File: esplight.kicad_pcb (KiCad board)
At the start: 2 copper layers, 14 parts, among them P1 CONN_01X03, P2 CONN_01X04, U1 AMS1117, U2 ESP-201

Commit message: got the board to a more or less finished state - gonna try variants now
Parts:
- removed USB1: BARREL_JACK, Connect:USB_Micro-B
- added P3: USB_B, Connect:USB_Micro-B, F.Cu at (27.9, 59.7)
- R1, R2, R3, R4: value 20kE -> 10kE
- SW1: renamed from BOOT; value DIPS_03 -> BOOT
- SW2: renamed from RESET; value SW_PUSH -> RESET
- moved U1 6.48 mm to (30.5, 50.8), turned to 180 degrees
- moved C2 2.54 mm to (34.3, 39.4)
- moved R3 2.50 mm to (25.4, 24.1)
- moved R2 1.78 mm to (25.4, 26.7)
- moved R1 1.63 mm to (25.4, 29.2)
- moved P2 1.48 mm to (41.9, 34.3)
- moved P1 1.30 mm to (41.9, 16.5)
- moved R4 1.27 mm to (25.4, 31.8)
- moved SW2 1.27 mm to (41.9, 43.2)
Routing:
- net GND: track 155.8 -> 137.4 mm
- net /3.3V: track 68.1 -> 55.1 mm
- net Net-(R1-Pad1): track 33.6 -> 40.2 mm
- net Net-(R3-Pad1): track 43.3 -> 48.3 mm
- net /+5V: track 53.0 -> 57.1 mm
- net Net-(P1-Pad1): track 18.0 -> 20.8 mm
- net Net-(P1-Pad2): track 16.1 -> 18.3 mm
- net Net-(R4-Pad1): track 14.3 -> 16.5 mm
- net Net-(R2-Pad1): track 44.5 -> 43.5 mm
- net Net-(P2-Pad2): track 5.18 -> 6.13 mm
- net (no net): track 0.00 -> 0.76 mm
- net Net-(P2-Pad3): track 7.72 -> 7.18 mm
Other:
- board outline added: 34.3 x 48.3 mm
- rule via_min_drill: 0.3 -> 0.35
- board text added: "GPIO 0"
- board text added: "GPIO 2"
- board text added: "GPIO15"
- board text added: "GPIO2 GPIO0 GPIO15 H L L Download H H L Boot Flash X X H Boot SD"
- board text added: "LED Control"
- board text added: "RESET"
- board text added: "Serial"

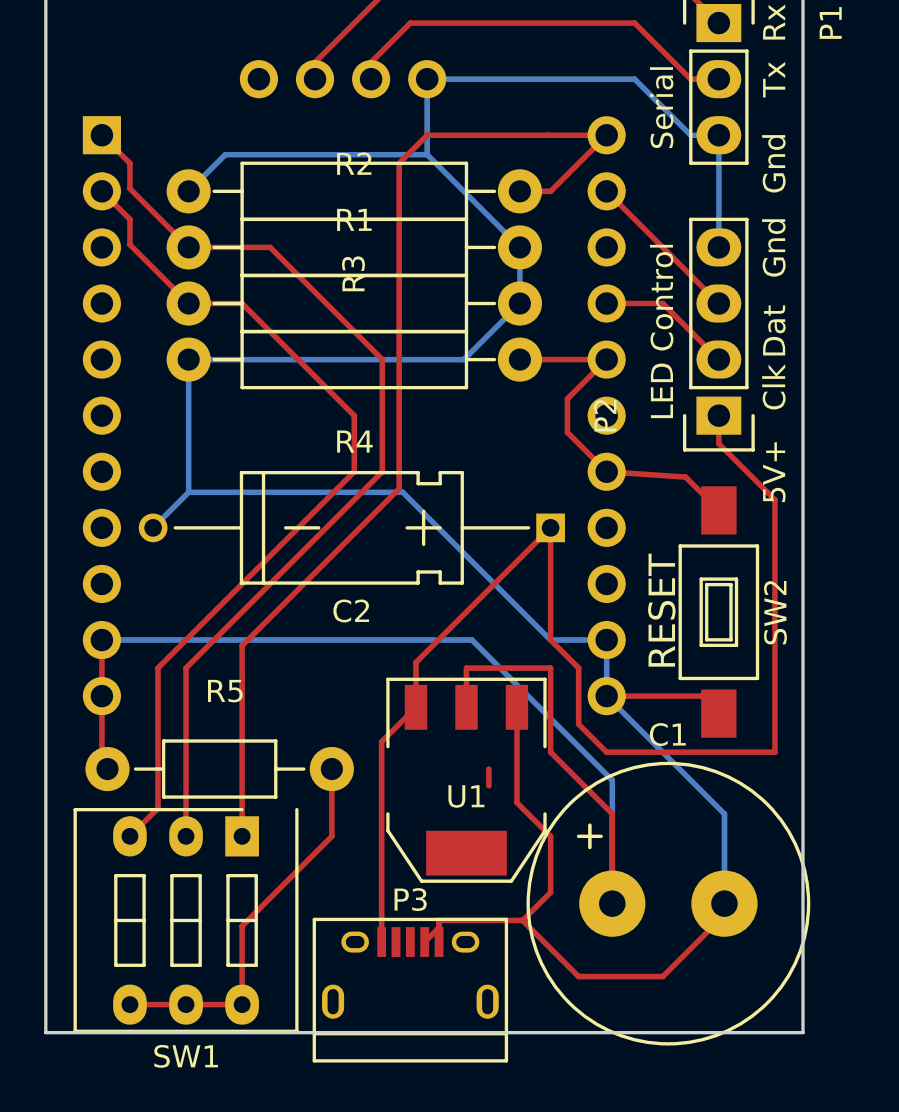
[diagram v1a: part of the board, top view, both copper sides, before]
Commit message: connecting chip_en pin, fixing some resistors
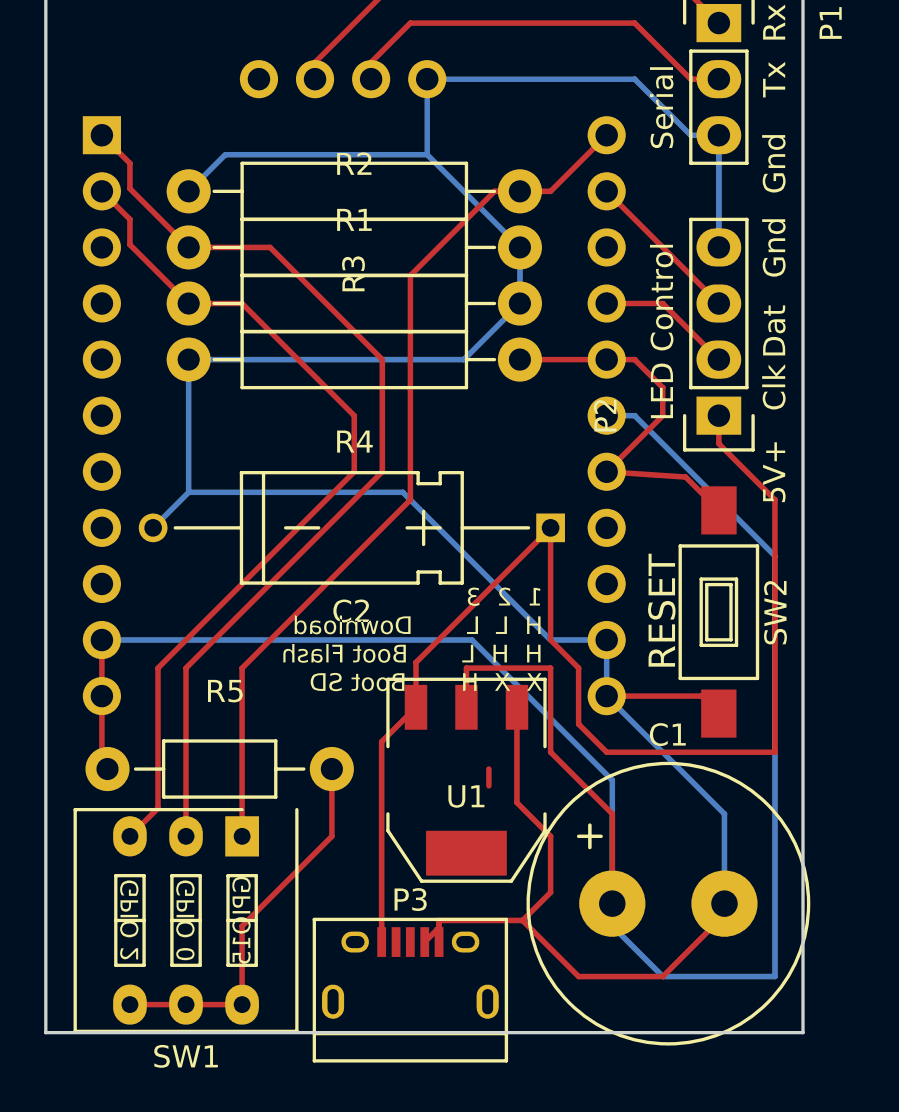
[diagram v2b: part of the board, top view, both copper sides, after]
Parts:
- R1, R2, R3, R4: value 10kE -> 1kE
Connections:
- U2 pad 17: /+3.3V -> /3.3V
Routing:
- net /3.3V: track 55.1 -> 93.7 mm
- net Net-(R3-Pad1): track 48.3 -> 40.1 mm
- net Net-(R4-Pad1): track 16.5 -> 17.9 mm
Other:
- board text added: "1 2 3 H L L Download H H L Boot Flash X X H Boot SD"
- board text removed: "GPIO2 GPIO0 GPIO15 H L L Download H H L Boot Flash X X H Boot SD"

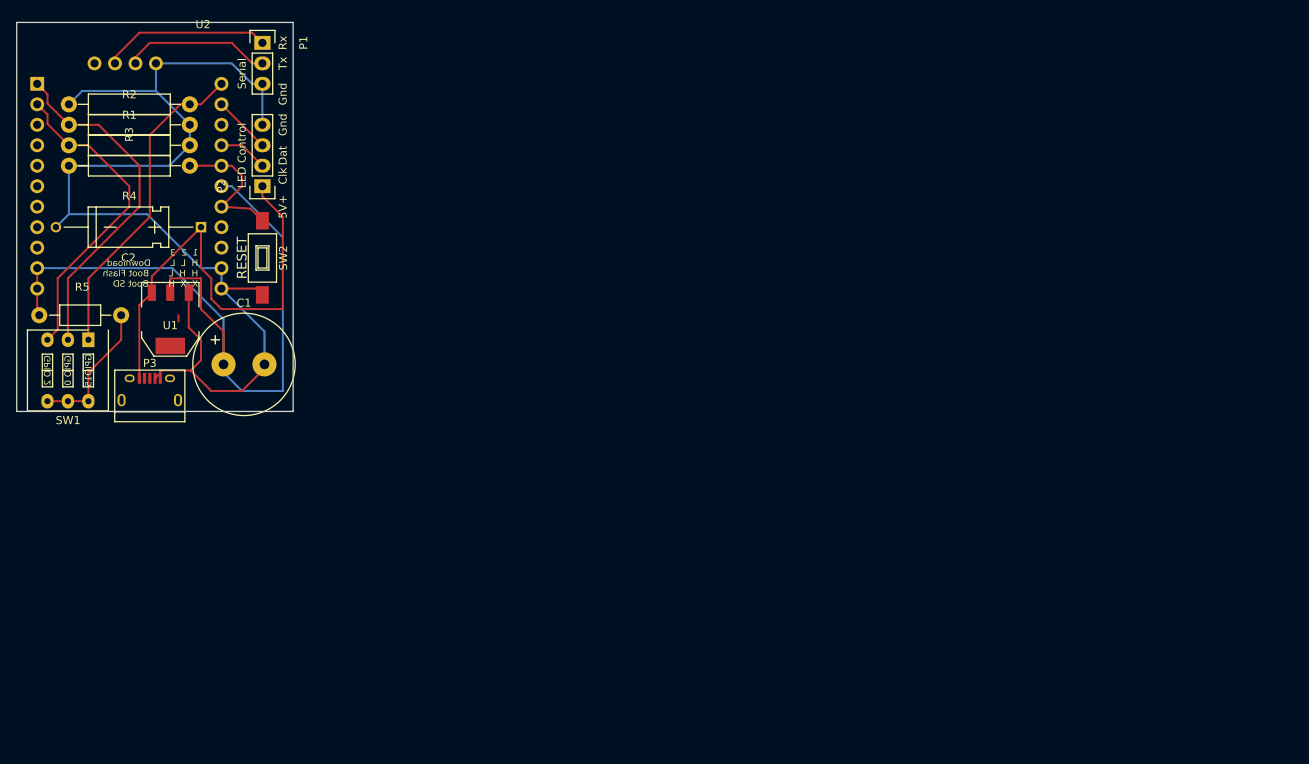
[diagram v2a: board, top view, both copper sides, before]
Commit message: Version 2 of the board - added USB/TTL and more SMT
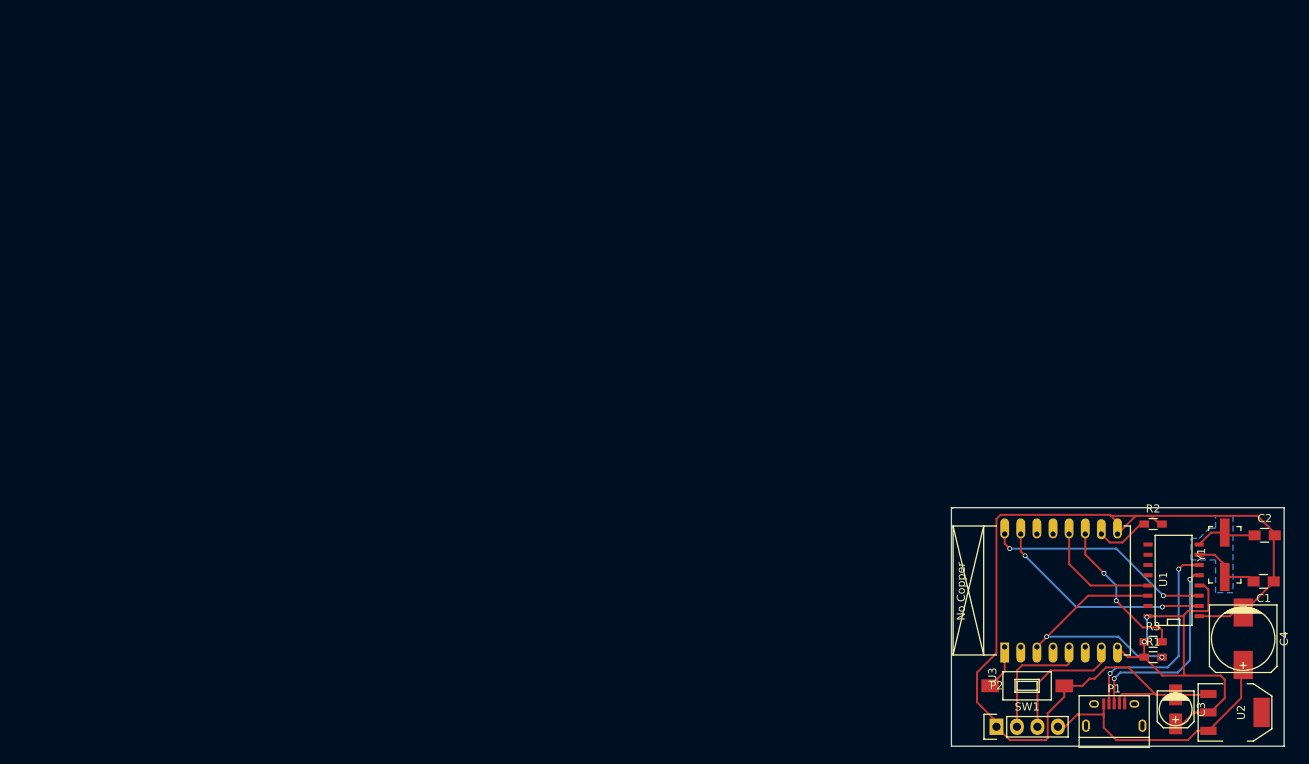
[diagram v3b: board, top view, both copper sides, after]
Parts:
- removed P3: USB_B, Connect:USB_Micro-B
- removed R4: 1kE, Resistors_ThroughHole:Resistor_Horizontal_RM15mm
- removed R5: 100E, Resistors_ThroughHole:Resistor_Horizontal_RM10mm
- removed SW2: RESET, Buttons_Switches_SMD:SW_SPST_FSMSM
- added C3: 22uF, Capacitors_SMD:c_elec_4x5.8, F.Cu at (155.2, 99.2)
- added C4: 470uF, Capacitors_SMD:c_elec_8x10, F.Cu at (163.6, 90.4)
- added U3: ESP-07v2, ESP8266:ESP-07v2, F.Cu at (134.0, 91.4)
- added Y1: 20MHz, Rager:Crystal_CSM-3X_SMD, F.Cu at (161.3, 80.0)
- C1: value 1000uF -> 22pF; footprint Capacitors_Elko_ThroughHole:Elko_vert_25x12.5mm_RM5 -> Capacitors_SMD:C_0805_HandSoldering
- C2: value 100uF -> 22pF; footprint Capacitors_ThroughHole:C_Axial_D5_L11_P18 -> Capacitors_SMD:C_0805_HandSoldering
- P1: value CONN_01X03 -> USB_B; footprint Socket_Strips:Socket_Strip_Straight_1x03 -> Connect:USB_Micro-B
- R1, R2, R3: value 1kE -> 10kE; footprint Resistors_ThroughHole:Resistor_Horizontal_RM15mm -> Resistors_SMD:R_0603_HandSoldering
- SW1: value BOOT -> SW_PUSH; footprint Buttons_Switches_ThroughHole:SW_DIP_x3_Slide -> Buttons_Switches_SMD:SW_SPST_FSMSM
- U1: value AMS1117 -> CH340G; footprint TO_SOT_Packages_SMD:SOT-223 -> SMD_Packages:SO-16-N
- U2: value ESP-201 -> AMS1117; footprint ESP8266:ESP-201 -> TO_SOT_Packages_SMD:SOT-223
- moved U2 167.8 mm to (162.6, 99.6), turned to 270 degrees
- moved R3 143.4 mm to (152.4, 90.8), turned to 0 degrees
- moved R1 142.0 mm to (152.4, 92.7)
- moved C2 137.4 mm to (166.2, 77.6), turned to 0 degrees
- moved R2 136.3 mm to (152.4, 76.2)
- moved P1 134.7 mm to (147.6, 100.1), turned to 0 degrees
- moved C1 131.8 mm to (166.1, 83.3), turned to 180 degrees
- moved U1 128.6 mm to (154.9, 83.2), turned to 90 degrees
- moved SW1 124.1 mm to (136.8, 96.3)
- moved P2 113.1 mm to (133.0, 101.3), turned to 0 degrees
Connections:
- C1 pad 1: /3.3V -> /GND
- C1 pad 2: GND -> Net-(C1-Pad2)
- C2 pad 1: /+5V -> Net-(C2-Pad1)
- C2 pad 2: GND -> /GND
- P1 pad 1: Net-(P1-Pad1) -> /5V
- P1 pad 3: GND -> Net-(P1-Pad3)
- P2 pad 1: /+5V -> /GND
- P2 pad 2: Net-(P2-Pad2) -> /CLOCK
- P2 pad 3: Net-(P2-Pad3) -> /MOSI
- P2 pad 4: GND -> /5V
- R1 pad 1: Net-(R1-Pad1) -> /3.3V
- R1 pad 2: GND -> /RTS
- R2 pad 2: GND -> /GND
- R3 pad 1: Net-(R3-Pad1) -> /3.3V
- R3 pad 2: GND -> Net-(R3-Pad2)
- SW1 pad 1: Net-(R3-Pad1) -> /GND
- SW1 pad 2: Net-(R2-Pad1) -> /RESET
- U1 pad 1: GND -> /GND
- U1 pad 2: /3.3V -> /TX
- U1 pad 3: /+5V -> /RX
- U1 pad 4: (no net) -> /3.3V
- U2 pad 1: Net-(R2-Pad1) -> /GND
- U2 pad 2: Net-(R1-Pad1) -> /3.3V
- U2 pad 3: Net-(U2-Pad3) -> /5V
- U2 pad 4: Net-(U2-Pad4) -> (no net)
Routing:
- net GND: track 137.4 -> 0.00 mm
- net /GND: track 0.00 -> 130.6 mm
- net /+5V: track 57.1 -> 0.00 mm
- net /3.3V: track 93.7 -> 49.2 mm, vias 0 -> 2
- net Net-(R1-Pad1): track 40.2 -> 0.00 mm
- net Net-(R3-Pad1): track 40.1 -> 0.00 mm
- net Net-(R2-Pad1): track 43.5 -> 6.70 mm
- net /5V: track 0.00 -> 33.3 mm
- net /RTS: track 0.00 -> 31.8 mm, vias 0 -> 2
- net /RX: track 0.00 -> 28.0 mm, vias 0 -> 2
- net /TX: track 0.00 -> 27.2 mm, vias 0 -> 2
- net Net-(P1-Pad3): track 0.00 -> 25.1 mm, vias 0 -> 2
- net Net-(P1-Pad1): track 20.8 -> 0.00 mm
- net Net-(R3-Pad2): track 0.00 -> 18.5 mm, vias 0 -> 2
- net Net-(R4-Pad1): track 17.9 -> 0.00 mm
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- added copper zone on B.Cu, net /GND
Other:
- board size 34.3 x 48.3 mm -> 41.3 x 29.6 mm
- rule via_min_drill: 0.35 -> 0.3
- board text removed: "1 2 3 H L L Download H H L Boot Flash X X H Boot SD"
- board text removed: "5V+"
- board text removed: "Clk"
- board text removed: "Dat"
- board text removed: "GPIO 0"
- board text removed: "GPIO 2"
- board text removed: "GPIO15"
- board text removed: "Gnd"
- board text removed: "LED Control"
- board text removed: "RESET"
- board text removed: "Rx"
- board text removed: "Serial"
- board text removed: "Tx"
